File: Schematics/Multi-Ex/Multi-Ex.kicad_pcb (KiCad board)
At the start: 4 copper layers, 173 x 57 mm, 89 parts, among them IC2 ATF1508AS-7AX100, J1 DIN41612_02x32_AC(CAPS), J16 Conn_01x03, J2 Conn_01x03, J4 Conn_02x05_Odd_Even, J5 Conn_01x03, J6 Conn_02x05_Odd_Even, Q1 STL9P3LLH6, U1 MC68882_PLCC_68, U10 TXS0102DCT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

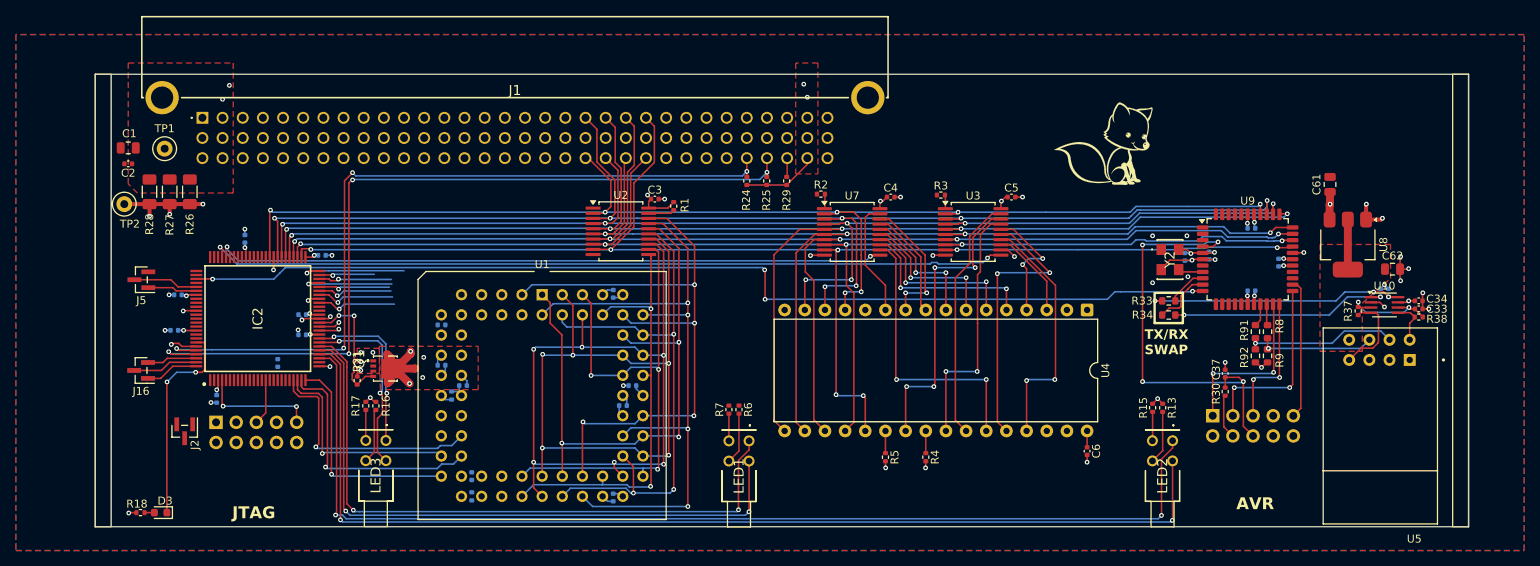
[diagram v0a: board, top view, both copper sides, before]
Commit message: Multi-expansion card routed.
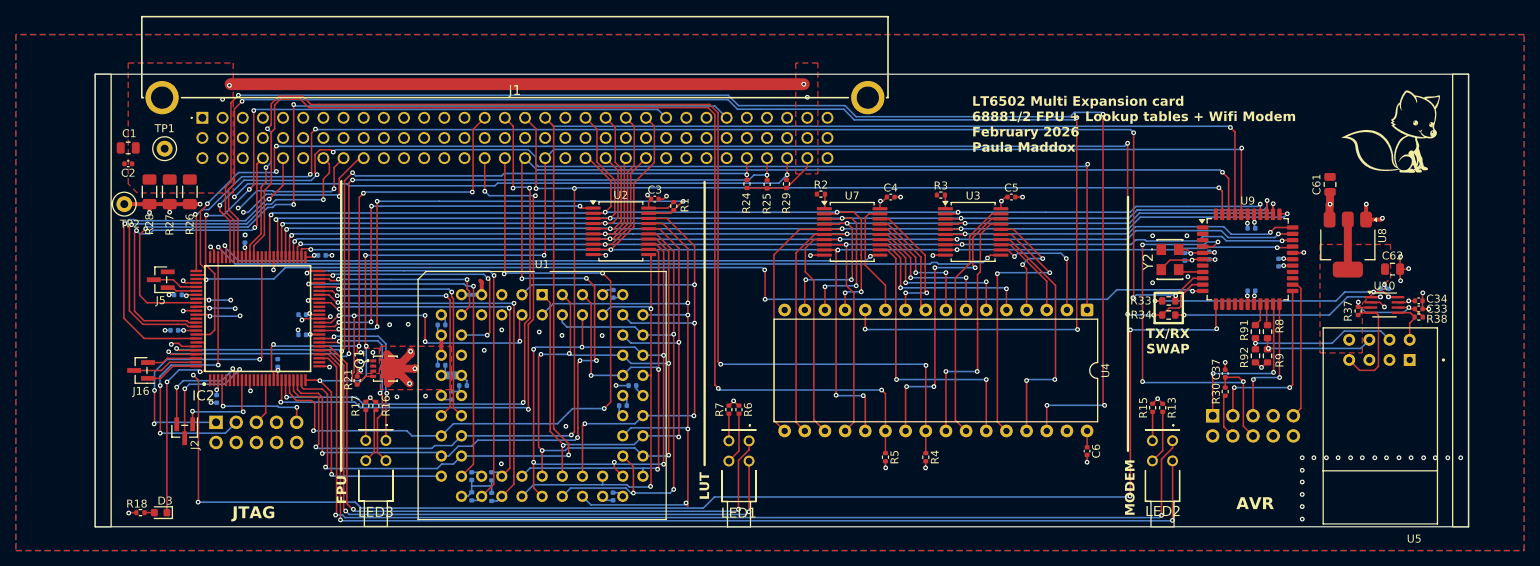
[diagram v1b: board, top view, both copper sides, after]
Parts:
- added R10: 10K, Resistor_SMD:R_0402_1005Metric, B.Cu at (119.9, 123.2)
- added R11: 10K, Resistor_SMD:R_0402_1005Metric, B.Cu at (119.9, 120.7)
- moved FOX1 36.2 mm to (233.9, 77.2)
- moved J5 2.44 mm to (78.2, 95.9)
- moved R25 0.43 mm to (154.6, 83.9)
- moved R29 0.38 mm to (157.1, 83.8)
- moved R24 0.38 mm to (152.1, 83.8)
- moved C21 0.13 mm to (135.2, 123.2)
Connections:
- IC2 pad 92: unconnected-(IC2-I/O_66-Pad92) -> /Connector/RDY
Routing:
- net /GLUE/MODEM_RnW: track 0.00 -> 183.8 mm, vias 0 -> 6
- net /GLUE/LUT_RES_HnL: track 0.00 -> 183.2 mm, vias 0 -> 4
- net /GLUE/LUT_FUNC0: track 0.00 -> 179.1 mm, vias 0 -> 4
- net /Modem/RX_5V: track 4.99 -> 164.4 mm, vias 0 -> 6
- net /Connector/A2: track 27.0 -> 185.7 mm, vias 1 -> 7
- net /Modem/TX_5V: track 7.46 -> 165.2 mm, vias 0 -> 6
- net /Connector/A1: track 31.6 -> 186.9 mm, vias 1 -> 3
- net /Connector/A0: track 28.2 -> 180.9 mm, vias 1 -> 6
- net /GLUE/LUT_nOE: track 2.79 -> 147.2 mm, vias 0 -> 4
- net /Connector/A3: track 30.3 -> 174.5 mm, vias 1 -> 5
- net /GLUE/LUT_FUNC1: track 0.00 -> 141.3 mm, vias 0 -> 4
- net /GLUE/LUT_nCS: track 2.79 -> 140.3 mm, vias 0 -> 2
- net /Connector/nIRQ: track 0.00 -> 104.0 mm, vias 0 -> 3
- net /Connector/A4: track 0.00 -> 92.1 mm, vias 0 -> 4
- net /Connector/EXP_nSEL: track 2.39 -> 91.4 mm, vias 0 -> 4
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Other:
- board text added: "FPU"
- board text added: "LT6502 Multi Expansion card 68881/2 FPU + Lookup tables + Wifi Modem February 2026 Paula Maddox"
- board text added: "LUT"
- board text added: "MODEM"
